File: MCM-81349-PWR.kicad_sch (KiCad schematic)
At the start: 22 parts, among them J10 JACK-L-LKWGPC-5A(R), U1 AZ1117CR-3.3TRG1, U2 LMR16006YDDCR

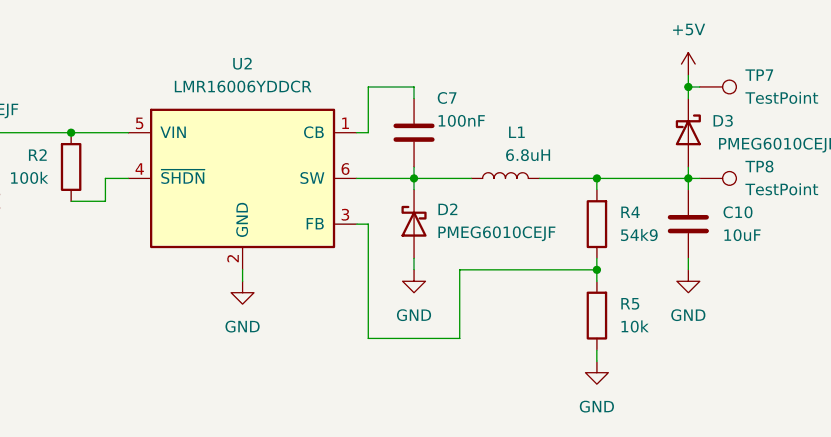
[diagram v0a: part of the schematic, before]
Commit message: use LV2862XDDC instead of LMR16006YQ
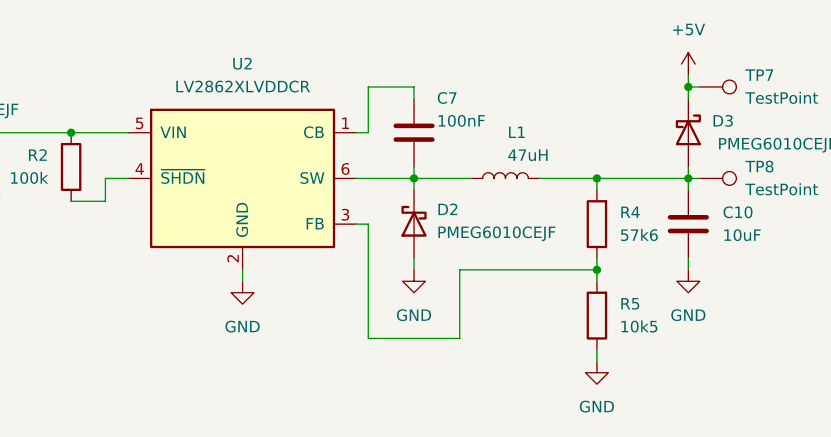
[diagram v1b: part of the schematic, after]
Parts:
- removed U2: LMR16006YDDCR, Package_TO_SOT_SMD:SOT-23-6, symbol Regulator_Switching:LMR16006YQ
- added U2: LV2862XLVDDCR, Package_TO_SOT_SMD:SOT-23-6, symbol Regulator_Switching:LV2862XDDC
- L1: value 6.8uH -> 47uH
- R4: value 54k9 -> 57k6
- R5: value 10k -> 10k5
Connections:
- net GND: now also U2.2 (GND)
- net at R2.1: now also U2.4 (~{SHDN})
- net at C1.1, D9.1 (K), R2.2: now also U2.5 (VIN)
- net at C7.1: now also U2.1 (CB)
- net at R4.1, R5.2: now also U2.3 (FB)
- net at C7.2, D2.1 (K), L1.1: now also U2.6 (SW)
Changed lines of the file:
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@@
-	)
-	(symbol
-		(lib_id "Regulator_Switching:LMR16006YQ")
-		(at 116.84 81.28 0)
-		(unit 1)
-		(exclude_from_sim no)
-		(in_bom yes)
-		(on_board yes)
-		(dnp no)
-		(fields_autoplaced yes)
-		(property "Reference" "U2"
-			(at 116.84 68.58 0)
-			(effects
-				(font
-					(size 1.27 1.27)
-				)
-			)
-		)
-		(property "Value" "LMR16006YDDCR"
-			(at 116.84 71.12 0)
-			(effects
-				(font
-					(size 1.27 1.27)
-				)
-			)
-		)
-		(property "Footprint" "Package_TO_SOT_SMD:SOT-23-6"
-			(at 116.84 93.98 0)
-			(effects
-				(font
-					(size 1.27 1.27)
-					(italic yes)
-				)
-				(hide yes)
-			)
-		)
-		(property "Datasheet" "http://www.ti.com/lit/ds/symlink/lmr16006y-q1.pdf"
-			(at 106.68 69.85 0)
-			(effects
-				(font
-					(size 1.27 1.27)
-				)
-				(hide yes)
-			)
-		)
-		(property "Description" "Simple Switcher Buck Regulator, Vin=4-40V, Iout=600mA, Adjustable output voltage, SOT-23-6 package"
-			(at 116.84 81.28 0)
-			(effects
-				(font
-					(size 1.27 1.27)
-				)
-				(hide yes)
-			)
-		)
-		(pin "1"
-		)
-		(pin "2"
-		)
-		(pin "3"
-		)
-		(pin "4"
-		)
-		(pin "5"
-		)
-		(pin "6"
-		)
-		(instances
-			(project "MCM-81349"
-				(path "/10a668bb-e341-4631-a862-dadf8a9a10bc/72c7d519-8696-4dcf-8164-31de870ed890"
-					(reference "U2")
-					(unit 1)
-				)
-			)
-		)
 	)
 	(symbol
@@
 	)
 	(symbol
+		(lib_id "Regulator_Switching:LV2862XDDC")
+		(at 116.84 81.28 0)
+		(unit 1)
+		(exclude_from_sim no)
+		(in_bom yes)
+		(on_board yes)
+		(dnp no)
+		(fields_autoplaced yes)
+		(property "Reference" "U2"
+			(at 116.84 68.58 0)
+			(effects
+				(font
+					(size 1.27 1.27)
+				)
+			)
+		)
+		(property "Value" "LV2862XLVDDCR"
+			(at 116.84 71.12 0)
+			(effects
+				(font
+					(size 1.27 1.27)
+				)
+			)
+		)
+		(property "Footprint" "Package_TO_SOT_SMD:SOT-23-6"
+			(at 116.84 93.98 0)
+			(effects
+				(font
+					(size 1.27 1.27)
+					(italic yes)
+				)
+				(hide yes)
+			)
+		)
+		(property "Datasheet" "https://www.ti.com/lit/ds/symlink/lv2862.pdf"
+			(at 106.68 69.85 0)
+			(effects
+				(font
+					(size 1.27 1.27)
+				)
+				(hide yes)
+			)
+		)
+		(property "Description" "60V, 0.6A, stepdown, DC/DC converter, 770kHz"
+			(at 116.84 81.28 0)
+			(effects
+				(font
+					(size 1.27 1.27)
+				)
+				(hide yes)
+			)
+		)
+		(pin "3"
+		)
+		(pin "5"
+		)
+		(pin "6"
+		)
+		(pin "4"
+		)
+		(pin "2"
+		)
+		(pin "1"
+		)
+		(instances
+			(project "MCM-81349"
+				(path "/10a668bb-e341-4631-a862-dadf8a9a10bc/72c7d519-8696-4dcf-8164-31de870ed890"
+					(reference "U2")
+					(unit 1)
+				)
+			)
+		)
+	)
+	(symbol
 		(lib_id "Device:D_Schottky")
 		(at 81.28 76.2 180)
@@
 			)
 		)
-		(property "Value" "6.8uH"
+		(property "Value" "47uH"
 			(at 148.59 78.74 90)
 			(effects
@@
 			)
 		)
-		(property "Description" "HPC 4018NF-6R8M"
+		(property "Description" "HPC4018NF-470M"
 			(at 146.05 81.28 0)
 			(effects
@@
 			)
 		)
-		(property "Value" "10k"
+		(property "Value" "10k5"
 			(at 158.75 97.7899 0)
 			(effects
@@
 			)
 		)
-		(property "Description" "RES SMD 10K OHM 1% 1/16W 0402"
+		(property "Description" "RES SMD 10K5 OHM 1% 1/16W 0402"
 			(at 156.21 96.52 0)
 			(effects
@@
 			)
 		)
-		(property "Value" "54k9"
+		(property "Value" "57k6"
 			(at 158.75 87.6299 0)
 			(effects
@@
 			)
 		)
-		(property "Description" "RES 54.9K OHM 1% 1/16W 0402"
+		(property "Description" "RES 57.6K OHM 1% 1/16W 0402"
 			(at 156.21 86.36 0)
 			(effects

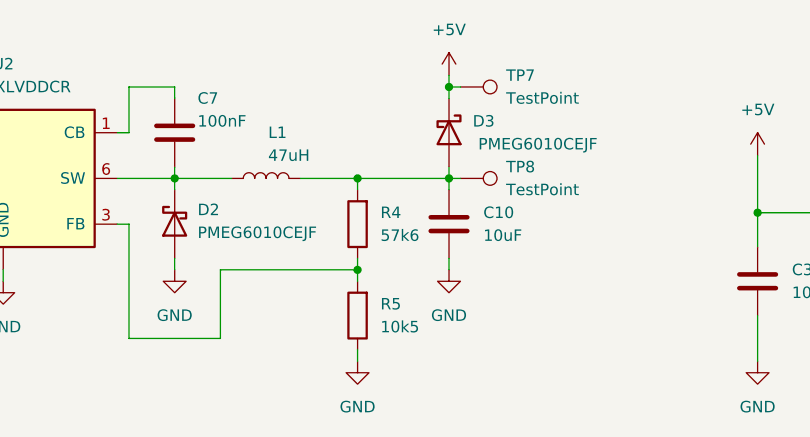
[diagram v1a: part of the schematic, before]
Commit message: update output voltage to be above vusb
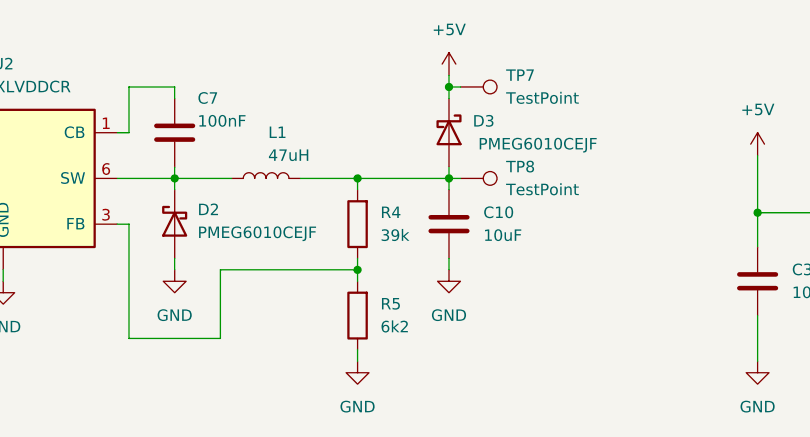
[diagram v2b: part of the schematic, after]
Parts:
- R4: value 57k6 -> 39k
- R5: value 10k5 -> 6k2
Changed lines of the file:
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@@
 			)
 		)
-		(property "Value" "10k5"
+		(property "Value" "6k2"
 			(at 158.75 97.7899 0)
 			(effects
@@
 			)
 		)
-		(property "Value" "57k6"
+		(property "Value" "39k"
 			(at 158.75 87.6299 0)
 			(effects

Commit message: replace coil with digikey available version
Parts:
- L1: footprint extra:HPC4018NF-Series -> Extra:WE-LQS
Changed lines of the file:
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@@
 			)
 		)
-		(property "Footprint" "extra:HPC4018NF-Series"
+		(property "Footprint" "Extra:WE-LQS"
 			(at 146.05 81.28 0)
 			(effects
@@
 			)
 		)
-		(property "Datasheet" "https://www.tai-tech.com.tw/pdf/263710/HPC4018NF-SERIES.pdf"
+		(property "Datasheet" "https://www.we-online.com/components/products/datasheet/74404042470.pdf"
 			(at 146.05 81.28 0)
 			(effects
@@
 			)
 		)
-		(property "Description" "HPC4018NF-470M"
+		(property "Description" "74404042470"
 			(at 146.05 81.28 0)
 			(effects
